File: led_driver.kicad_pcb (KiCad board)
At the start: 2 copper layers, 10.2 x 15.7 mm, 3 parts, among them P1 CONN_01X02, U1 AL5809-15P1-7

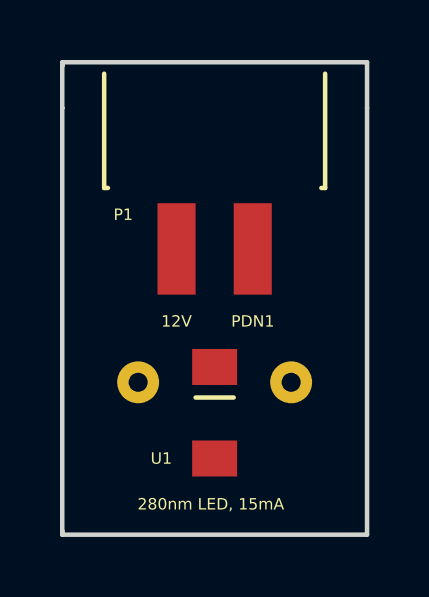
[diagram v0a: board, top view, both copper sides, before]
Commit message: Update silk screen
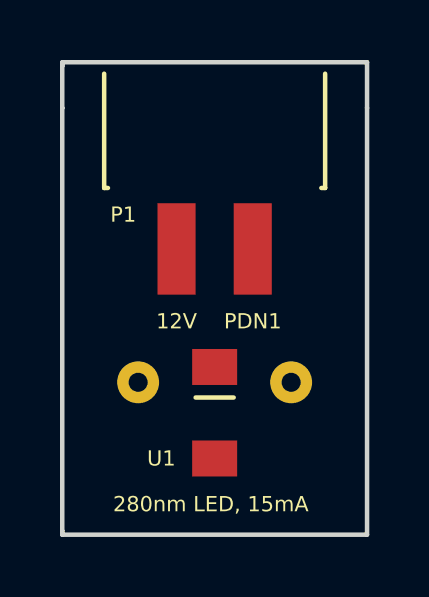
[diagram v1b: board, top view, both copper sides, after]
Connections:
- net /+V renamed /12V
- net /-V renamed /PDN1
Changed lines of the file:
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@@
     (pcb_text_size 1.5 1.5)
     (mod_edge_width 0.15)
-    (mod_text_size 0.381 0.381)
-    (mod_text_width 0.0762)
+    (mod_text_size 0.508 0.508)
+    (mod_text_width 0.127)
     (pad_size 1.524 1.524)
     (pad_drill 0.762)
@@
   (net 0 "")
   (net 1 "Net-(D1-Pad1)")
-  (net 2 /+V)
-  (net 3 /-V)
+  (net 2 /12V)
+  (net 3 /PDN1)
   (net_class Default "This is the default net class."
     (clearance 0.1524)
@@
     (uvia_dia 0.3)
     (uvia_drill 0.1)
-    (add_net /+V)
-    (add_net /-V)
+    (add_net /12V)
+    (add_net /PDN1)
     (add_net "Net-(D1-Pad1)")
   )
@@
     (descr "TO-5, 2PIN")
     (tags "TO-5, 2PIN, TO-5-2")
-    (fp_text reference D1 (at -0.0254 -0.254 180) (layer B.SilkS)
-      (effects (font (size 0.381 0.381) (thickness 0.0762)) (justify mirror))
+    (fp_text reference D1 (at 0 5.461 180) (layer B.SilkS)
+      (effects (font (size 0.508 0.508) (thickness 0.127)) (justify mirror))
     )
     (fp_text value MTE280H33-UV (at -0.0254 -4.064 180) (layer B.Fab)
-      (effects (font (size 0.381 0.381) (thickness 0.0762)) (justify mirror))
+      (effects (font (size 0.508 0.508) (thickness 0.127)) (justify mirror))
     )
     (fp_line (start -4.064 4.064) (end -3.81 4.318) (layer B.SilkS) (width 0.15))
@@
       (net 1 "Net-(D1-Pad1)"))
     (pad 2 thru_hole circle (at 2.55 0 180) (size 1.397 1.397) (drill 0.635) (layers *.Cu *.Mask B.SilkS)
-      (net 2 /+V))
+      (net 2 /12V))
   )
   (module jnod_footprints:Sullins_M89_1X2 (layer F.Cu)
     (at 132.715 103.886)
     (fp_text reference P1 (at -1.778 -1.143) (layer F.SilkS)
-      (effects (font (size 0.381 0.381) (thickness 0.0762)))
+      (effects (font (size 0.508 0.508) (thickness 0.127)))
     )
     (fp_text value CONN_01X02 (at 1.524 -7.993) (layer F.Fab)
-      (effects (font (size 0.381 0.381) (thickness 0.0762)))
+      (effects (font (size 0.508 0.508) (thickness 0.127)))
     )
     (fp_line (start 4.953 -2.032) (end 4.826 -2.032) (layer F.SilkS) (width 0.15))
@@
     (fp_line (start -2.159 -6.096) (end 4.699 -6.096) (layer Dwgs.User) (width 0.0762))
     (pad 1 smd rect (at 0 0) (size 1.27 3.048) (layers F.Cu F.Paste F.Mask)
-      (net 2 /+V))
+      (net 2 /12V))
     (pad 2 smd rect (at 2.54 0) (size 1.27 3.048) (layers F.Cu F.Paste F.Mask)
-      (net 3 /-V))
+      (net 3 /PDN1))
   )
   (module jnod_footprints:PowerDI-123_B (layer F.Cu)
     (at 133.985 110.871 90)
     (fp_text reference U1 (at 0 -1.778 180) (layer F.SilkS)
-      (effects (font (size 0.381 0.381) (thickness 0.0762)))
+      (effects (font (size 0.508 0.508) (thickness 0.127)))
     )
     (fp_text value AL5809-15P1-7 (at 2.056 -2.436 90) (layer F.Fab)
-      (effects (font (size 0.381 0.381) (thickness 0.0762)))
+      (effects (font (size 0.508 0.508) (thickness 0.127)))
     )
     (fp_line (start 2.032 -0.635) (end 2.032 0.635) (layer F.SilkS) (width 0.15))
@@
       (net 1 "Net-(D1-Pad1)"))
     (pad 2 smd rect (at 3.05 0 90) (size 1.2 1.5) (layers F.Cu F.Paste F.Mask)
-      (net 3 /-V))
+      (net 3 /PDN1))
   )
   (gr_text "280nm LED, 15mA" (at 133.858 112.395) (layer F.SilkS)
-    (effects (font (size 0.381 0.381) (thickness 0.0762)))
+    (effects (font (size 0.508 0.508) (thickness 0.127)))
   )
   (gr_line (start 139.065 97.663) (end 139.065 99.187) (angle 90) (layer Edge.Cuts) (width 0.15))
@@
   (gr_line (start 128.905 99.187) (end 128.905 97.79) (angle 90) (layer Edge.Cuts) (width 0.15))
   (gr_text PDN1 (at 135.255 106.299) (layer F.SilkS)
-    (effects (font (size 0.381 0.381) (thickness 0.0762)))
+    (effects (font (size 0.508 0.508) (thickness 0.127)))
   )
   (gr_text 12V (at 132.715 106.299) (layer F.SilkS)
-    (effects (font (size 0.381 0.381) (thickness 0.0762)))
+    (effects (font (size 0.508 0.508) (thickness 0.127)))
   )
   (gr_line (start 128.905 113.411) (end 139.065 113.411) (angle 90) (layer Edge.Cuts) (width 0.15))

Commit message: Remove gerbers from repo
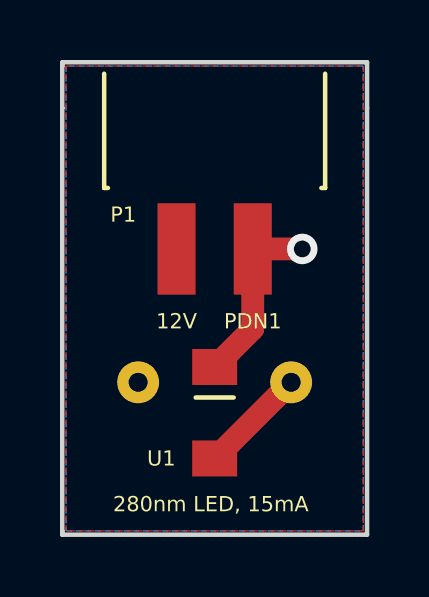
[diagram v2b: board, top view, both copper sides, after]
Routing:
- net /PDN1: track 0.00 -> 6.11 mm, vias 0 -> 1
- net Net-(D1-Pad1): track 0.21 -> 3.81 mm
- added copper zone on F.Cu, net /12V
- added copper zone on B.Cu, net /PDN1
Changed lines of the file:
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@@
   (general
     (links 3)
-    (no_connects 3)
-    (area 128.829999 97.587999 139.140001 113.486001)
+    (no_connects 0)
+    (area 128.829999 95.1945 139.140001 113.486001)
     (thickness 1.6)
     (drawings 11)
-    (tracks 1)
+    (tracks 7)
     (zones 0)
     (modules 3)
@@
   )
   (setup
-    (last_trace_width 0.1524)
+    (last_trace_width 0.762)
     (user_trace_width 0.381)
     (user_trace_width 0.762)
     (trace_clearance 0.1524)
-    (zone_clearance 0.2032)
+    (zone_clearance 0.254)
     (zone_45_only no)
     (trace_min 0.1524)
@@
       (drillshape 0)
       (scaleselection 1)
-      (outputdirectory gerber/))
+      (outputdirectory led_driver_gbr/))
   )
   (net 0 "")
@@
   (gr_line (start 139.065 99.187) (end 139.065 113.411) (angle 90) (layer Edge.Cuts) (width 0.15))
   (gr_line (start 128.905 113.284) (end 128.905 99.187) (angle 90) (layer Edge.Cuts) (width 0.15))
+  (segment (start 133.985 110.871) (end 133.995 110.871) (width 0.762) (layer F.Cu) (net 1) (status C00000))
+  (segment (start 133.995 110.871) (end 136.535 108.331) (width 0.762) (layer F.Cu) (net 1) (status C00000))
   (segment (start 136.535 108.2675) (end 136.535 108.4795) (width 0.762) (layer F.Cu) (net 1))
+  (segment (start 135.255 103.886) (end 135.255 106.551) (width 0.762) (layer F.Cu) (net 3) (status 400000))
+  (segment (start 135.255 106.551) (end 133.985 107.821) (width 0.762) (layer F.Cu) (net 3) (status 800000))
+  (segment (start 135.255 103.886) (end 136.906 103.886) (width 0.762) (layer F.Cu) (net 3) (status 400000))
+  (via (at 136.906 103.886) (size 1.016) (drill 0.5588) (layers F.Cu B.Cu) (net 3))
+  (zone (net 2) (net_name /12V) (layer F.Cu) (hatch edge 0.508)
+    (connect_pads yes (clearance 0.254))
+    (min_thickness 0.2286)
+    (fill yes (arc_segments 16) (thermal_gap 0.508) (thermal_bridge_width 0.508))
+    (polygon
+      (pts
+        (xy 129.032 97.79) (xy 138.938 97.79) (xy 138.938 113.284) (xy 129.032 113.284)
+      )
+    )
+  )
+  (zone (net 3) (net_name /PDN1) (layer B.Cu) (hatch edge 0.508)
+    (connect_pads yes (clearance 0.254))
+    (min_thickness 0.2286)
+    (fill yes (arc_segments 16) (thermal_gap 0.508) (thermal_bridge_width 0.508))
+    (polygon
+      (pts
+        (xy 129.032 113.284) (xy 138.938 113.284) (xy 138.938 97.79) (xy 129.032 97.79)
+      )
+    )
+  )
 )
